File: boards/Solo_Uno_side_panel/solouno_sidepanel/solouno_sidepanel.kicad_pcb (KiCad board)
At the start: 2 copper layers, 20 x 72 mm, 10 parts, among them CN1 CAN Front, CN2 CAN Back

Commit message: Updated Solon
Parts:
- added hole1: MountingHole_2.2mm_M2_Pad, MountingHole:MountingHole_2.2mm_M2_Pad, F.Cu at (153.4, 159.9)
- added hole2: MountingHole_2.2mm_M2_Pad, MountingHole:MountingHole_2.2mm_M2_Pad, F.Cu at (131.0, 159.9)
- added hole3: MountingHole_2.2mm_M2_Pad, MountingHole:MountingHole_2.2mm_M2_Pad, F.Cu at (131.0, 104.3)
- added hole4: MountingHole_2.2mm_M2_Pad, MountingHole:MountingHole_2.2mm_M2_Pad, F.Cu at (153.4, 104.3)
- A2: footprint Connector_PinHeader_2.54mm:PinHeader_1x03_P2.54mm_Vertical -> Connector_JST:JST_EH_B3B-EH-A_1x03_P2.50mm_Vertical
- C1: footprint Capacitor_THT:CP_Radial_D4.0mm_P1.50mm -> Capacitor_THT:C_Rect_L4.0mm_W2.5mm_P2.50mm
- CN1, CN2, PW1, PW2: footprint Connector_PinHeader_2.54mm:PinHeader_1x02_P2.54mm_Vertical -> Connector_JST:JST_EH_B2B-EH-A_1x02_P2.50mm_Vertical
- E1, E2: footprint Connector_PinHeader_2.54mm:PinHeader_1x05_P2.54mm_Vertical -> Connector_JST:JST_EH_B5B-EH-A_1x05_P2.50mm_Vertical
- moved CN2 27.4 mm to (146.1, 130.7), turned to 90 degrees
- moved CN1 27.4 mm to (138.2, 130.7), turned to 90 degrees
- moved E2 21.2 mm to (153.5, 130.7), turned to 90 degrees
- moved A2 20.2 mm to (144.2, 116.5), turned to 180 degrees
- moved E1 16.2 mm to (130.5, 130.7)
- moved PW1 15.7 mm to (134.0, 138.3), turned to 0 degrees
- moved PW2 12.6 mm to (149.8, 138.3), turned to 180 degrees
- moved S1 7.86 mm to (135.0, 143.8)
- moved C1 7.84 mm to (142.0, 137.3)
- moved A1 5.69 mm to (141.9, 155.5)
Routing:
- net Net-(A2-Pin_2): track 68.6 -> 43.5 mm
- net Net-(A2-Pin_3): track 71.2 -> 50.5 mm
- net Net-(A2-Pin_1): track 67.3 -> 48.9 mm
- net Net-(E1-Pin_2): track 7.55 -> 24.0 mm
- net Net-(E1-Pin_3): track 6.75 -> 23.0 mm
- net Net-(E1-Pin_1): track 8.41 -> 24.0 mm
- net Net-(E1-Pin_4): track 7.69 -> 23.0 mm
- net Net-(E1-Pin_5): track 8.07 -> 23.0 mm
- net +28V: track 14.9 -> 0.00 mm
- net GND: track 13.5 -> 0.00 mm
- net Net-(PW2-Pin_2): track 14.4 -> 6.09 mm, vias 1 -> 0
- net Net-(S1-Pin_3): track 5.94 -> 4.84 mm
- net Net-(PW2-Pin_1): track 8.33 -> 8.90 mm
- added copper zone on F.Cu, net +28V
- added copper zone on B.Cu, net GND
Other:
- board size 20 x 72 mm -> 30 x 65 mm
- board text added: "ROBOJACKET"
- board text added: "TX"
- board text added: "URC Solouno v1"

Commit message: side panel with Gerber
waiting for final aviation dimensions
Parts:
- moved A2 27.8 mm to (144.6, 144.3)
- moved C1 8.19 mm to (142.1, 129.1)
- moved PW1 8.19 mm to (134.1, 130.1)
- moved PW2 8.19 mm to (149.9, 130.1)
- moved S1 8.19 mm to (135.1, 135.6)
- moved CN1 8.19 mm to (138.3, 122.5)
- moved CN2 8.19 mm to (146.2, 122.5)
- moved E1 8.19 mm to (130.6, 122.5)
- moved E2 8.19 mm to (153.6, 122.5)
- moved A1 0.24 mm to (142.1, 155.6)
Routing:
- net Net-(A2-Pin_1): track 48.9 -> 10.9 mm
- net Net-(A2-Pin_3): track 50.5 -> 18.4 mm
- net Net-(A2-Pin_2): track 43.5 -> 17.9 mm

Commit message: side panel
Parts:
- removed hole1, hole2, hole3, hole4: MountingHole_2.2mm_M2_Pad, MountingHole:MountingHole_2.2mm_M2_Pad
- moved E2 92.2 mm to (62.0, 132.8), turned to 0 degrees
- moved A2 90.6 mm to (69.5, 93.6)
- moved A1 89.7 mm to (67.0, 106.6)
- moved PW1 83.3 mm to (58.0, 96.1), turned to 90 degrees
- moved PW2 81.4 mm to (76.0, 96.1), turned to 90 degrees
- moved CN2 79.5 mm to (68.3, 138.2), turned to 180 degrees
- moved C1 74.8 mm to (68.3, 116.6), turned to 180 degrees
- moved E1 71.8 mm to (62.0, 143.7), turned to 0 degrees
- moved CN1 70.2 mm to (68.3, 126.0), turned to 180 degrees
- moved S1 68.7 mm to (73.9, 166.7), turned to 180 degrees
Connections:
- C1 pad 2: Net-(S1-Pin_3) -> GND
- PW2 pad 2: Net-(PW2-Pin_2) -> GND
- S1 pad 3: Net-(S1-Pin_3) -> Net-(PW2-Pin_1)
- S1 pad 4: Net-(PW2-Pin_2) -> GND
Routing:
- net Net-(PW2-Pin_1): track 8.90 -> 86.1 mm
- net Net-(E1-Pin_2): track 24.0 -> 10.8 mm
- net Net-(E1-Pin_1): track 24.0 -> 10.8 mm
- net Net-(E1-Pin_5): track 23.0 -> 10.8 mm
- net Net-(E1-Pin_4): track 23.0 -> 10.8 mm
- net Net-(E1-Pin_3): track 23.0 -> 10.8 mm
- net Net-(PW2-Pin_2): track 6.09 -> 0.00 mm
- net Net-(S1-Pin_3): track 4.84 -> 0.00 mm
- net Net-(CN1-Pin_2): track 7.89 -> 12.2 mm
- net Net-(CN1-Pin_1): track 7.89 -> 12.2 mm
- net Net-(A2-Pin_1): track 10.9 -> 12.5 mm
- net Net-(A2-Pin_3): track 18.4 -> 20.1 mm
- net Net-(A2-Pin_2): track 17.9 -> 19.1 mm
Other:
- board size 30 x 65 mm -> 29 x 80 mm
- board text removed: "RX"
- board text removed: "TX"

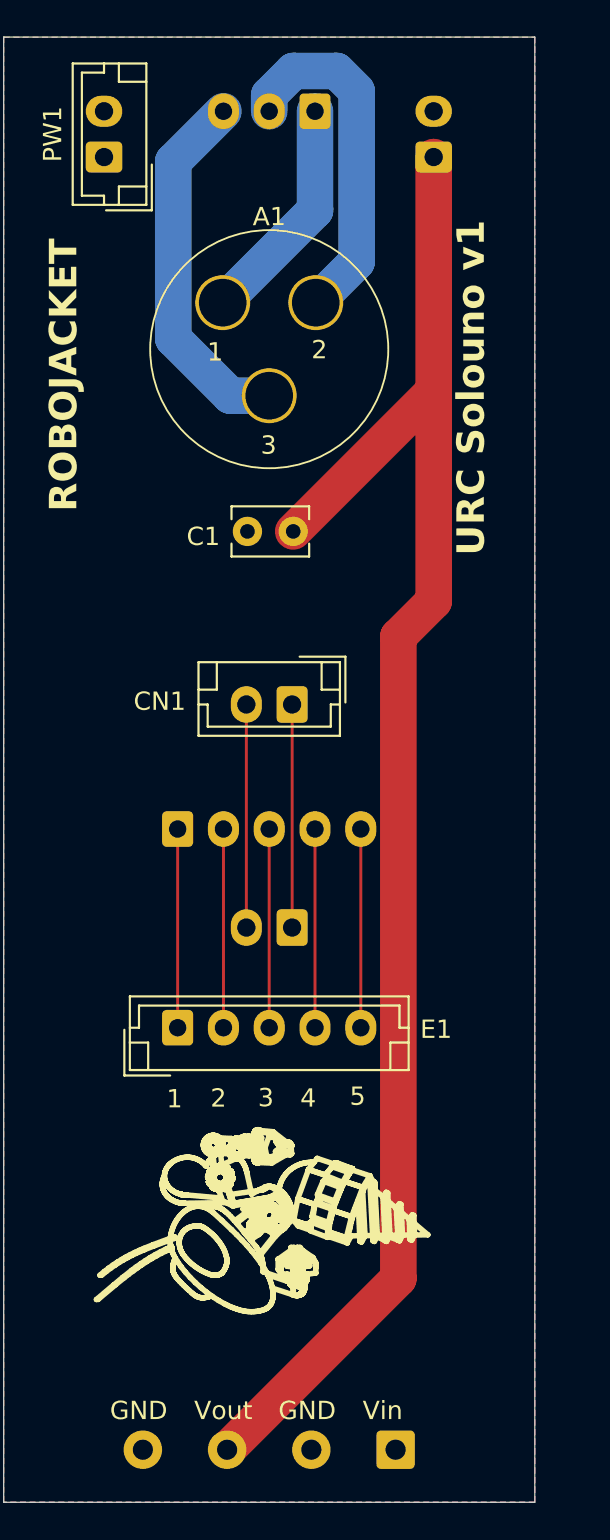
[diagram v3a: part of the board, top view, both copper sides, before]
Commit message: updated solouno with new footprint
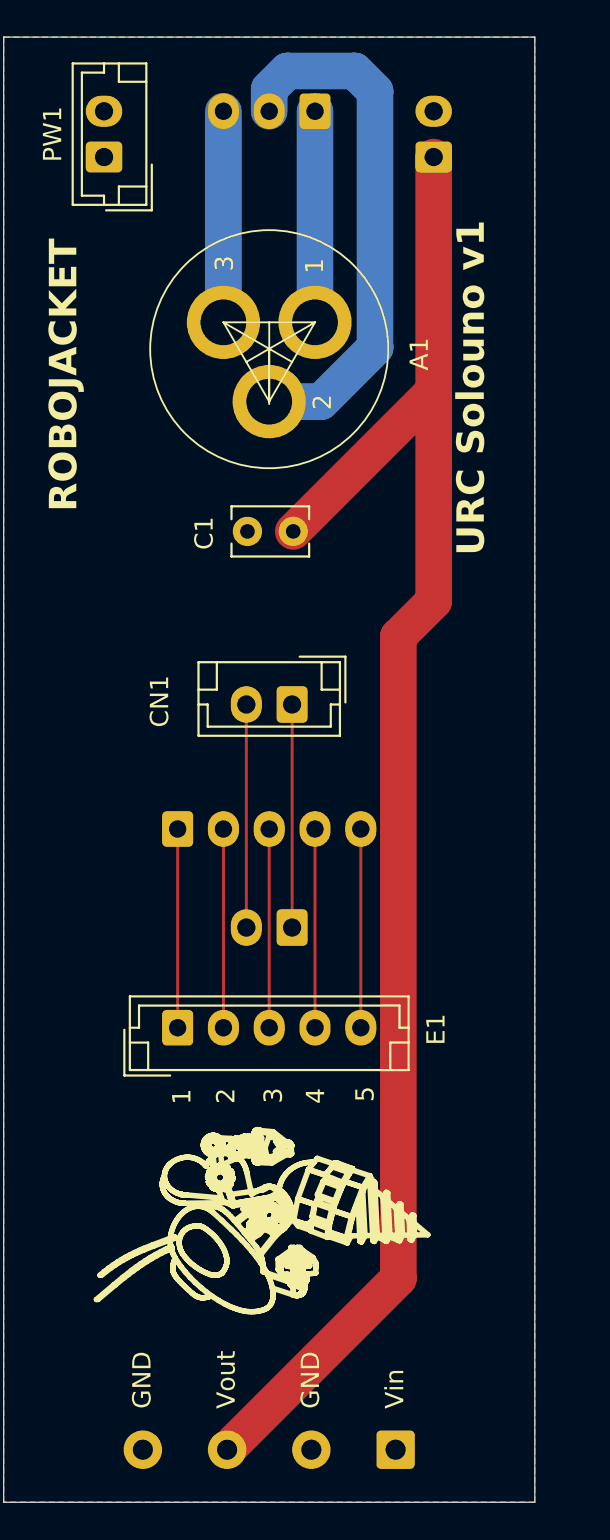
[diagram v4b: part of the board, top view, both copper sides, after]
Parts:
- A1: footprint Library:GX-16-3 -> Connector:GX-16-3
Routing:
- net Net-(A2-Pin_2): track 19.1 -> 28.9 mm
- net Net-(A2-Pin_3): track 20.1 -> 11.5 mm
- net Net-(A2-Pin_1): track 12.5 -> 11.5 mm
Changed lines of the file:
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@@
 		(tags "connector JST EH vertical")
 		(property "Reference" "CN1"
-			(at 7.23 0.17 180)
+			(at 7.23 0.17 -90)
 			(layer "F.SilkS")
 			(effects
@@
 		(tags "C Rect series Radial pin pitch 2.50mm  length 4mm width 2.5mm Capacitor")
 		(property "Reference" "C1"
-			(at 4.91 -0.28 180)
+			(at 4.86 -0.1 -90)
 			(layer "F.SilkS")
 			(effects
@@
 		(tags "connector JST EH vertical")
 		(property "Reference" "E1"
-			(at 14.11 0.09 180)
+			(at 14.11 0.09 -90)
 			(layer "F.SilkS")
 			(effects
@@
 		)
 	)
-	(footprint "Library:GX-16-3"
+	(footprint "Connector:GX-16-3"
 		(layer "F.Cu")
 		(at 67.01 106.62)
 		(property "Reference" "A1"
-			(at 0 -7.229998 0)
+			(at 8.2 0.26 90)
 			(unlocked yes)
 			(layer "F.SilkS")
@@
 				(font
 					(size 1 1)
-					(thickness 0.153)
+					(thickness 0.154)
 				)
 			)
@@
 			)
 		)
-		(property "Footprint" "Library:GX-16-3"
+		(property "Footprint" "Connector:GX-16-3"
 			(at 0 0 0)
 			(unlocked yes)
@@
 		(sheetfile "solouno_sidepanel.kicad_sch")
 		(attr smd)
+		(fp_line
+			(start -2.5 -1.465063)
+			(end 0 2.865064)
+			(stroke
+				(width 0.1)
+				(type default)
+			)
+			(layer "F.SilkS")
+		)
+		(fp_line
+			(start -2.5 -1.465063)
+			(end 1.25 0.7)
+			(stroke
+				(width 0.1)
+				(type default)
+			)
+			(layer "F.SilkS")
+		)
+		(fp_line
+			(start 0 0)
+			(end 0 3)
+			(stroke
+				(width 0.1)
+				(type default)
+			)
+			(layer "F.SilkS")
+		)
+		(fp_line
+			(start 0 2.865064)
+			(end 0 -1.465063)
+			(stroke
+				(width 0.1)
+				(type default)
+			)
+			(layer "F.SilkS")
+		)
+		(fp_line
+			(start 0 2.865064)
+			(end 2.5 -1.465063)
+			(stroke
+				(width 0.1)
+				(type default)
+			)
+			(layer "F.SilkS")
+		)
+		(fp_line
+			(start 2.5 -1.465063)
+			(end -2.5 -1.465063)
+			(stroke
+				(width 0.1)
+				(type default)
+			)
+			(layer "F.SilkS")
+		)
+		(fp_line
+			(start 2.5 -1.465063)
+			(end -1.25 0.7)
+			(stroke
+				(width 0.1)
+				(type default)
+			)
+			(layer "F.SilkS")
+		)
 		(fp_circle
 			(center 0 0)
@@
 		)
 		(pad "1" thru_hole circle
-			(at -2.54 -2.54)
-			(size 3 3)
-			(drill 2.6)
+			(at 2.5 -1.465063)
+			(size 4 4)
+			(drill 2.5)
 			(layers "*.Cu" "*.Mask")
 			(remove_unused_layers no)
@@
 		)
 		(pad "2" thru_hole circle
-			(at 2.54 -2.54)
-			(size 3 3)
-			(drill 2.6)
+			(at 0 2.865064)
+			(size 4 4)
+			(drill 2.5)
 			(layers "*.Cu" "*.Mask")
 			(remove_unused_layers no)
@@
 		)
 		(pad "3" thru_hole circle
-			(at 0 2.54)
-			(size 3 3)
-			(drill 2.6)
+			(at -2.5 -1.465063)
+			(size 4 4)
+			(drill 2.5)
 			(layers "*.Cu" "*.Mask")
 			(remove_unused_layers no)
@@
 			(pintype "input")
 		)
+		(group ""
+			(members "25c6a0a0-f618-439a-b54b-d0cc19f205b5" "2a8c284c-7bf6-4734-8044-a1e93524ba8d"
+				"527123f7-0733-4f69-b240-5c86e2f34516" "a60e24e6-b625-4f14-ac06-5d9d69412c40"
+				"bd59b5d3-a7b1-4b18-9679-1e1b3947dfa7" "e42210c0-3974-47b3-9949-54177d754267"
+			)
+		)
 	)
 	(footprint "Connector_JST:JST_EH_B3B-EH-A_1x03_P2.50mm_Vertical"
@@
 		(tags "connector JST EH vertical")
 		(property "Reference" "E2"
-			(at 14.2 -0.3 0)
+			(at 14.2 -0.3 180)
 			(layer "B.SilkS")
 			(effects
@@
 		(tags "connector JST EH vertical")
 		(property "Reference" "PW2"
-			(at 1.25 2.8 90)
+			(at -4.1 0.04 180)
 			(layer "B.SilkS")
 			(effects
@@
 	)
 	(gr_text "Vout"
-		(at 62.91 165.16 0)
+		(at 65.25 164.48 90)
 		(layer "F.SilkS")
 		(effects
@@
 	)
 	(gr_text "2"
-		(at 63.8 148.1 0)
+		(at 65.23 147.83 90)
 		(layer "F.SilkS")
 		(effects
@@
 	)
 	(gr_text "GND"
-		(at 67.51 165.16 0)
+		(at 69.85 164.48 90)
 		(layer "F.SilkS")
 		(effects
@@
 	)
 	(gr_text "2"
-		(at 69.31 107.24 -0)
+		(at 70.5 109.95 90)
 		(layer "F.SilkS")
 		(effects
@@
 	)
 	(gr_text "5"
-		(at 71.4 148 0)
+		(at 72.83 147.73 90)
 		(layer "F.SilkS")
 		(effects
@@
 	)
 	(gr_text "1"
-		(at 63.62 107.36 -0)
+		(at 70.08 102.51 90)
 		(layer "F.SilkS")
 		(effects
@@
 			(font
 				(size 1.5 1.5)
-				(thickness 0.25)
+				(thickness 0.26)
 				(bold yes)
 			)
@@
 	)
 	(gr_text "3"
-		(at 66.39 148.08 0)
+		(at 67.82 147.81 90)
 		(layer "F.SilkS")
 		(effects
@@
 	)
 	(gr_text "4"
-		(at 68.7 148.1 0)
+		(at 70.13 147.83 90)
 		(layer "F.SilkS")
 		(effects
@@
 	)
 	(gr_text "1"
-		(at 61.4 148.14 0)
+		(at 62.83 147.87 90)
 		(layer "F.SilkS")
 		(effects
@@
 	)
 	(gr_text "Vin"
-		(at 72.11 165.16 0)
+		(at 74.45 164.48 90)
 		(layer "F.SilkS")
 		(effects
@@
 	)
 	(gr_text "GND"
-		(at 58.31 165.16 0)
+		(at 60.65 164.48 90)
 		(layer "F.SilkS")
 		(effects
@@
 	)
 	(gr_text "3"
-		(at 66.54 112.45 -0)
+		(at 65.15 102.37 90)
 		(layer "F.SilkS")
 		(effects
@@
 	)
 	(segment
-		(start 61.77 96.37)
-		(end 61.77 106.04132)
-		(width 2)
-		(layer "B.Cu")
-		(net 1)
-	)
-	(segment
-		(start 61.77 106.04132)
-		(end 64.88868 109.16)
-		(width 2)
-		(layer "B.Cu")
-		(net 1)
-	)
-	(segment
-		(start 64.88868 109.16)
-		(end 67.01 109.16)
-		(width 2)
-		(layer "B.Cu")
-		(net 1)
-	)
-	(segment
 		(start 64.51 93.63)
-		(end 61.77 96.37)
+		(end 64.51 105.154937)
 		(width 2)
 		(layer "B.Cu")
@@
 	)
 	(segment
-		(start 68.327462 91.43)
-		(end 70.692538 91.43)
+		(start 67.01 92.42)
+		(end 67.01 93.63)
 		(width 2)
 		(layer "B.Cu")
@@
 	)
 	(segment
-		(start 71.78 92.517462)
-		(end 71.78 101.85)
+		(start 69.838427 109.485064)
+		(end 72.79 106.533491)
 		(width 2)
 		(layer "B.Cu")
@@
 	)
 	(segment
-		(start 67.01 92.747462)
-		(end 68.327462 91.43)
+		(start 68 91.43)
+		(end 67.01 92.42)
 		(width 2)
 		(layer "B.Cu")
@@
 	)
 	(segment
-		(start 67.01 93.63)
-		(end 67.01 92.747462)
+		(start 67.01 109.485064)
+		(end 69.838427 109.485064)
 		(width 2)
 		(layer "B.Cu")
@@
 	)
 	(segment
-		(start 71.78 101.85)
-		(end 69.55 104.08)
+		(start 71.68 91.43)
+		(end 68 91.43)
 		(width 2)
 		(layer "B.Cu")
@@
 	)
 	(segment
-		(start 70.692538 91.43)
-		(end 71.78 92.517462)
+		(start 72.79 106.533491)
+		(end 72.79 92.54)
 		(width 2)
 		(layer "B.Cu")
@@
 	)
 	(segment
-		(start 69.51 99.04)
-		(end 64.47 104.08)
+		(start 72.79 92.54)
+		(end 71.68 91.43)
 		(width 2)
 		(layer "B.Cu")
-		(net 5)
+		(net 4)
 	)
 	(segment
 		(start 69.51 93.63)
-		(end 69.51 99.04)
+		(end 69.51 105.154937)
 		(width 2)
 		(layer "B.Cu")

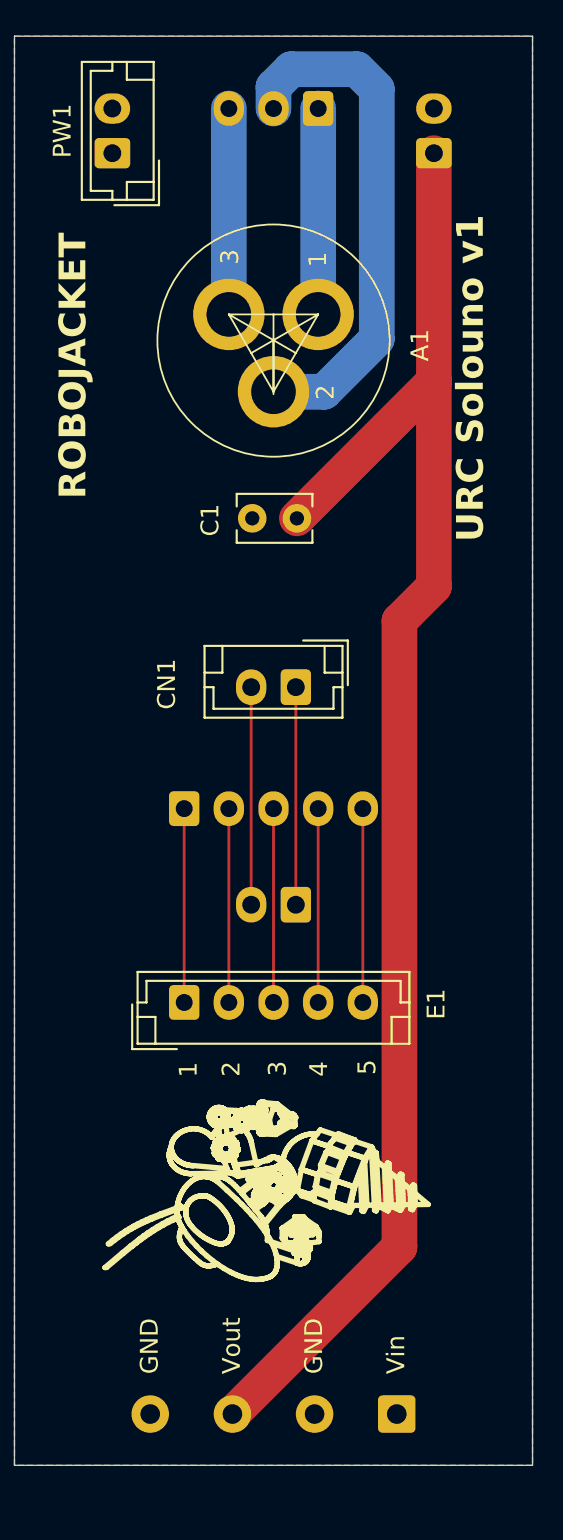
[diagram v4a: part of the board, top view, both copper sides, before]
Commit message: updated Solouno
Two pin for rocker switch
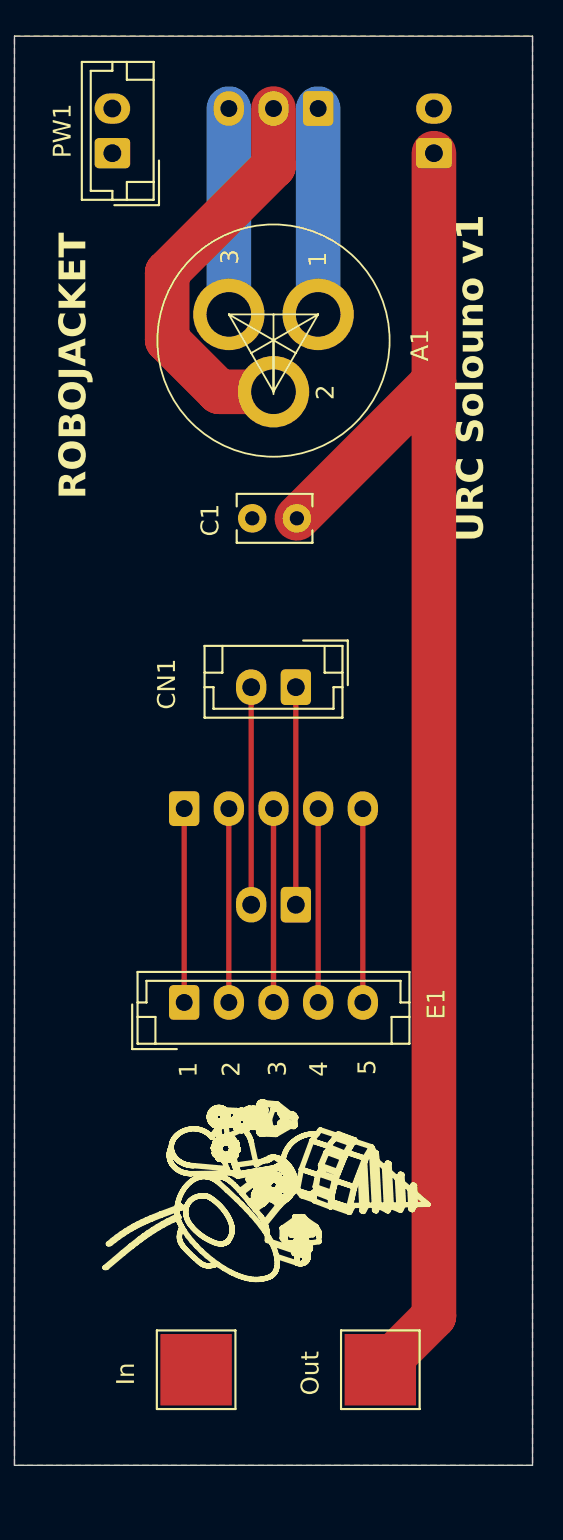
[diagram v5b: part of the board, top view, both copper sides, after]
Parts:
- added S2: Output, TestPoint:TestPoint_Pad_4.0x4.0mm, F.Cu at (73.0, 164.2)
- S1: value Pin -> Input; footprint Connector_Wire:SolderWire-0.5sqmm_1x04_P4.6mm_D0.9mm_OD2.1mm -> TestPoint:TestPoint_Pad_4.0x4.0mm
- moved S1 11.5 mm to (62.7, 164.2), turned to 90 degrees
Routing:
- net Net-(A2-Pin_2): track 28.9 -> 22.6 mm
- net Net-(PW2-Pin_1): track 86.1 -> 80.2 mm
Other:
- board text added: "In"
- board text added: "Out"
- board text removed: "GND"
- board text removed: "Vin"
- board text removed: "Vout"

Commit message: solouno update
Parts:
- removed A2: Aviation Pin, Connector_JST:JST_EH_B3B-EH-A_1x03_P2.50mm_Vertical
- removed C1: 3.3uF, Capacitor_THT:C_Rect_L4.0mm_W2.5mm_P2.50mm
- added T1: Test1, TestPoint:TestPoint_Pad_1.5x1.5mm, F.Cu at (193.0, 124.6)
- added T2: Test2, TestPoint:TestPoint_Pad_1.5x1.5mm, F.Cu at (189.8, 124.5)
- added T3: Test3, TestPoint:TestPoint_Pad_1.5x1.5mm, F.Cu at (186.5, 124.4)
- S1, S2: footprint TestPoint:TestPoint_Pad_4.0x4.0mm -> TestPoint:TestPoint_Loop_D3.50mm_Drill1.4mm_Beaded
- moved S1 149.9 mm to (184.4, 76.8)
- moved S2 149.9 mm to (194.7, 76.8)
- moved CN2 132.1 mm to (190.9, 89.2)
- moved E1 129.6 mm to (184.5, 101.3)
- moved CN1 129.4 mm to (190.9, 84.8)
- moved E2 127.6 mm to (184.4, 97.0)
- moved PW2 125.5 mm to (198.8, 70.1)
- moved PW1 125.5 mm to (180.8, 70.1)
- moved A1 122.9 mm to (189.7, 114.1)
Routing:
- net Net-(PW2-Pin_1): track 80.2 -> 6.81 mm
- net Net-(A1-Pad2): track 22.6 -> 7.83 mm
- net Net-(CN1-Pin_2): track 12.2 -> 4.33 mm
- net Net-(CN1-Pin_1): track 12.2 -> 4.33 mm
- net Net-(E1-Pin_5): track 10.8 -> 4.34 mm
- net Net-(E1-Pin_4): track 10.8 -> 4.34 mm
- net Net-(E1-Pin_3): track 10.8 -> 4.34 mm
- net Net-(E1-Pin_2): track 10.8 -> 4.34 mm
- net Net-(E1-Pin_1): track 10.8 -> 4.34 mm
- net Net-(A1-Pad3): track 11.5 -> 13.1 mm
- net Net-(A1-Pad1): track 11.5 -> 12.2 mm
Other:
- board text added: "RoboJackets"
- board text removed: "ROBOJACKET"
